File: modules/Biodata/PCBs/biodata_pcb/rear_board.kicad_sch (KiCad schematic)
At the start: 7 parts, among them U1 NE555P

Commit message: Working on biodata layout and PCB
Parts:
- added A1: Arduino_Nano_v3.x, Module:Arduino_Nano, symbol MCU_Module:Arduino_Nano_v3.x
- added C4: 100nF, symbol Device:C
- added C5: 10uF, Capacitor_THT:CP_Radial_D4.0mm_P1.50mm, symbol Device:C_Polarized_US
- added J10: Eurorack_2x8_Power, Connector_IDC:IDC-Header_2x08_P2.54mm_Vertical, symbol FreeModular:Eurorack_2x8_Power
- added Q1, Q2: 2N3904, Package_TO_SOT_THT:TO-92L_Inline_Wide, symbol Device:Q_NPN_EBC
- added R4, R5, R6, R7: 100kΩ, Resistor_THT:R_Axial_DIN0207_L6.3mm_D2.5mm_P10.16mm_Horizontal, symbol Device:R
- added R8, R9: 1kΩ, Resistor_THT:R_Axial_DIN0207_L6.3mm_D2.5mm_P10.16mm_Horizontal, symbol Device:R
- added U2: MCP4922, Package_DIP:DIP-14_W7.62mm, symbol Analog_DAC:MCP4922
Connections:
- net +5V: now also A1.27 (+5V), C4.2, C5.1, J10.11 (+5v), J10.12 (+5v), U2.1 (Vdd), U2.11 (VrefB), U2.13 (VrefA), U2.9 (~{SHDN})
- net GND: now also A1.29 (GND), A1.4 (GND), C4.1, C5.2, J10.3 (GND), J10.4 (GND), J10.5 (GND), J10.6 (GND), J10.7 (GND), J10.8 (GND), Q1.1 (E), Q2.1 (E), R5.1, R7.1, U2.12 (Vss), U2.8 (~{LDAC})
- net pulse_out: now also A1.5 (D2)
- net probe_pos: now reaches R2.1
- net probe_neg: now reaches R3.1
- new net: Q1.2 (B), R4.2, R5.2
- new net: J10.1 (-12v), J10.2 (-12v)
- new net: J10.10 (+12v), J10.9 (+12v)
- new net: R9.1, U2.10 (VB)
- new net: R8.1, U2.14 (VA)
- new net: Q2.2 (B), R6.2, R7.2
- new net DAC_CS: A1.13 (D10), U2.3 (~{CS})
- new net SPI_SCK: A1.16 (D13), U2.4 (SCK)
- new net SPI_SDI: A1.14 (D11), U2.5 (SDI)
- new net cv_out_a: R8.2
- new net cv_out_b: R9.2
- new net density: A1.22 (A3)
- new net gate_in_a: R4.1
- new net gate_in_a_buffered: A1.6 (D3), Q1.3 (C)
- new net gate_in_b: R6.1
- new net gate_in_b_buffered: A1.7 (D4), Q2.3 (C)
- new net gate_out_a: A1.8 (D5)
- new net gate_out_b: A1.9 (D6)
- new net sensitivity: A1.21 (A2)
- new net slew_a: A1.23 (A4)
- new net slew_b: A1.24 (A5)
- new net spread_a: A1.25 (A6)
- new net spread_b: A1.26 (A7)
- no-connect marks 0 -> 15
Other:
- note added: "with internal pullup to 5v"
- moved on the sheet: C1, C2, C3, R1, R2, R3, U1

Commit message: v0.1 biodata pcb
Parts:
- removed C1: 10nF, symbol Device:C
- removed C2: 1nF, symbol Device:C
- removed C3: 100nF, symbol Device:C
- removed R1: 1kΩ, symbol Device:R
- removed R2, R3: 1MΩ, symbol Device:R
- removed U1: NE555P, Package_DIP:DIP-8_W7.62mm, symbol Timer:NE555P
- added C10, C11, C8, C9: 100pF, Capacitor_THT:C_Disc_D4.7mm_W2.5mm_P5.00mm, symbol Device:C_Small
- added C14, C5, C6, C7: 100nF, Capacitor_THT:C_Disc_D4.7mm_W2.5mm_P5.00mm, symbol Device:C
- added Q3, Q4: 2N3904, Package_TO_SOT_THT:TO-92L_Inline_Wide, symbol Device:Q_NPN_EBC
- added R18, R19, R20, R21, R30, R32: 1kΩ, Resistor_THT:R_Axial_DIN0207_L6.3mm_D2.5mm_P10.16mm_Horizontal, symbol Device:R
- added R22, R23, R24, R25, R26, R27, R28, R29, R31: 10kΩ, Resistor_THT:R_Axial_DIN0207_L6.3mm_D2.5mm_P10.16mm_Horizontal, symbol Device:R
- added U5: MCP4922, Package_DIP:DIP-14_W7.62mm, symbol Analog_DAC:MCP4922
- added U6: TL074, Package_DIP:DIP-14_W7.62mm, symbol Amplifier_Operational:TL074
- C4: footprint (none) -> Capacitor_THT:C_Disc_D4.7mm_W2.5mm_P5.00mm
- R8, R9: value 1kΩ -> 100kΩ
- renumbered C5 to C13, J10 to J13
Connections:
- net +5V: now also C5.2, C6.2, R30.2, U5.1 (Vdd), U5.11 (VrefB), U5.13 (VrefA), U5.9 (~{SHDN})
- net GND: now also R9.1, C14.2, C5.1, C6.1, C7.1, Q3.1 (E), Q4.1 (E), R22.1, R24.1, R26.1, R28.1, U5.12 (Vss), U5.8 (~{LDAC})
- net SPI_SCK: now also U5.4 (SCK)
- net SPI_SDI: now also U5.5 (SDI)
- net cv_out_a: now also R19.2, R25.2; no longer R8.2
- net cv_out_b: now also R20.2, R27.2; no longer R9.2
- net density: now also A1.20 (A1); no longer A1.22 (A3)
- net gate_out_a: now also A1.9 (D6); no longer A1.8 (D5)
- net gate_out_b: now also A1.10 (D7); no longer A1.9 (D6)
- net pulse_out: now also R32.2; no longer A1.5 (D2)
- net sensitivity: now also A1.19 (A0); no longer A1.21 (A2)
- net slew_a: now also A1.22 (A3); no longer A1.23 (A4)
- net spread_a: now also A1.21 (A2); no longer A1.25 (A6)
- net spread_b: now also A1.23 (A4); no longer A1.26 (A7)
- net gate_out_c: now reaches A1.11 (D8)
- net DAC_CS_1: now reaches A1.12 (D9)
- net DAC_CS_1: now also U2.3 (~{CS})
- net -12V: now reaches J13.1 (-12v), J13.2 (-12v)
- net -12V: now also C14.1, U6.4 (V+)
- net +12V: now reaches J13.10 (+12v), J13.9 (+12v)
- net +12V: now also C7.2, U6.11 (V-)
- net prescale_cv: now reaches U2.10 (VB)
- net prescale_cv: now also U6.3 (+); no longer R9.1
- net gate_in_c: now reaches R8.1
- net gate_in_c: no longer U2.14 (VA)
- net DAC_CS renamed DAC_CS_2
- net DAC_CS_2: now also U5.3 (~{CS}); no longer U2.3 (~{CS})
- new net: Q3.2 (B), R8.2, R9.2
- new net: C8.1, R22.2, R23.1, U6.2 (-)
- new net: C10.1, R26.2, R27.1, U6.9 (-)
- new net: Q4.2 (B), R31.1
- new net: C8.2, R18.1, U6.1
- new net: C9.1, R24.2, R25.1, U6.6 (-)
- new net: C9.2, R19.1, U6.7
- new net: C10.2, R20.1, U6.8
- new net: C11.1, R28.2, R29.1, U6.13 (-)
- new net: C11.2, R21.1, U6.14
- new net Isolated Section/pulse_out: R31.2
- new net cv_out: R18.2, R23.2
- new net cv_out_c: R21.2, R29.2
- new net gate_in_c_buffered: A1.8 (D5), Q3.3 (C)
- new net prescale_cv_a: U2.14 (VA), U6.5 (+)
- new net prescale_cv_b: U5.10 (VB), U6.10 (+)
- new net prescale_cv_c: U5.14 (VA), U6.12 (+)
- new net pulse_signal: A1.5 (D2), Q4.3 (C), R30.1, R32.1
- new net slew_c: A1.26 (A7)
- new net spread_c: A1.25 (A6)
- no-connect marks 15 -> 8
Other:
- added sheet Isolated Section (isolated_section.kicad_sch)
- company: (none) -> Free Modular
- title: (none) -> Biodata
- moved on the sheet: C13, C4, J13, U2

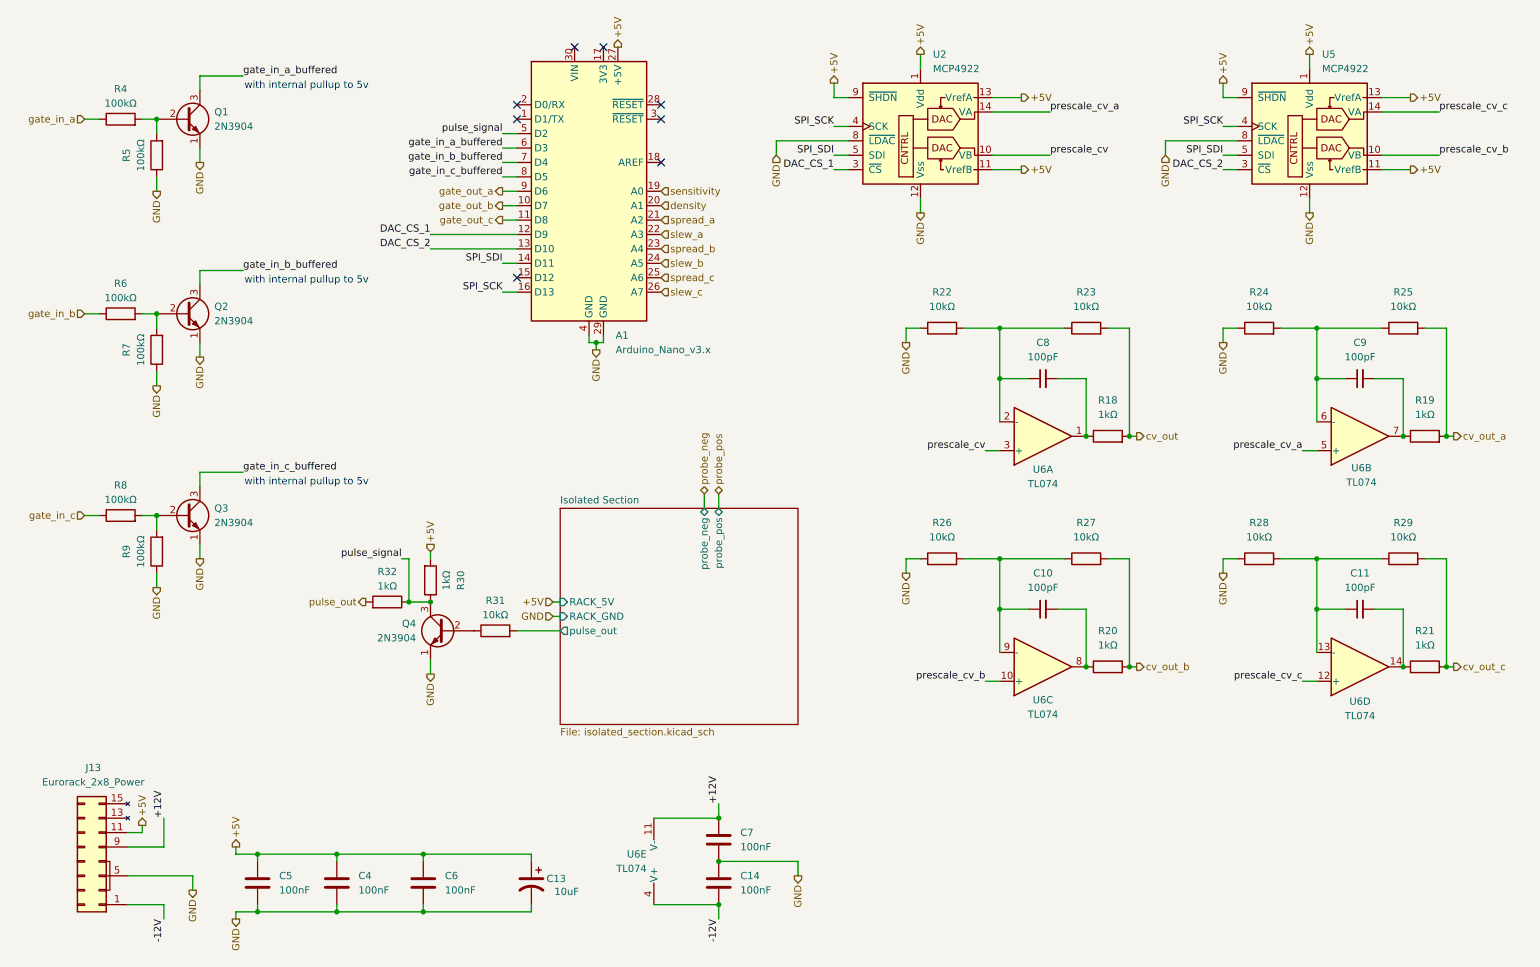
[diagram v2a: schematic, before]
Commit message: Switch biodata to monophonic
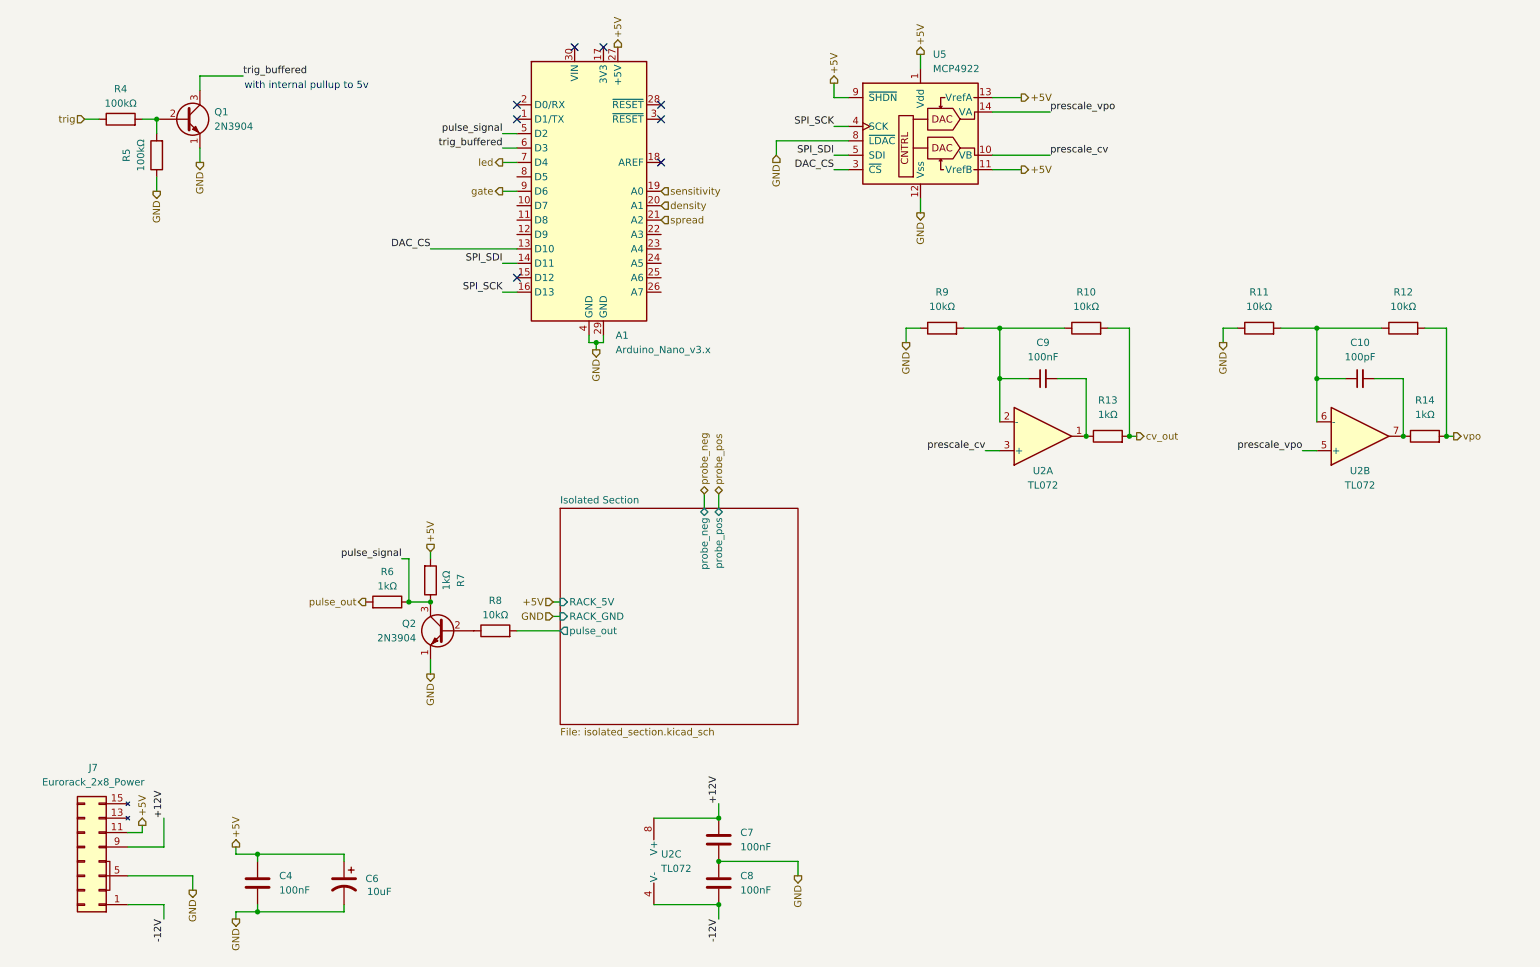
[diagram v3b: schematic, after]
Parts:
- removed C10, C11: 100pF, Capacitor_THT:C_Disc_D4.7mm_W2.5mm_P5.00mm, symbol Device:C_Small
- removed C4, C6: 100nF, Capacitor_THT:C_Disc_D4.7mm_W2.5mm_P5.00mm, symbol Device:C
- removed Q2, Q3: 2N3904, Package_TO_SOT_THT:TO-92L_Inline_Wide, symbol Device:Q_NPN_EBC
- removed R20, R21: 1kΩ, Resistor_THT:R_Axial_DIN0207_L6.3mm_D2.5mm_P10.16mm_Horizontal, symbol Device:R
- removed R26, R27, R28, R29: 10kΩ, Resistor_THT:R_Axial_DIN0207_L6.3mm_D2.5mm_P10.16mm_Horizontal, symbol Device:R
- removed R6, R7, R8, R9: 100kΩ, Resistor_THT:R_Axial_DIN0207_L6.3mm_D2.5mm_P10.16mm_Horizontal, symbol Device:R
- removed U5: MCP4922, Package_DIP:DIP-14_W7.62mm, symbol Analog_DAC:MCP4922
- removed U6: TL074, Package_DIP:DIP-14_W7.62mm, symbol Amplifier_Operational:TL074
- added U2: TL072, Package_DIP:DIP-8_W7.62mm, symbol Amplifier_Operational:TL072
- C9: renamed from C8; value 100pF -> 100nF
- renumbered C9 to C10, C5 to C4, C13 to C6, C14 to C8, J13 to J7, Q4 to Q2, R23 to R10, R24 to R11, R25 to R12, R18 to R13, R19 to R14, R32 to R6, R30 to R7, R31 to R8, R22 to R9, U2 to U5
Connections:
- net +12V: now also U2.8 (V+)
- net -12V: now also U2.4 (V-)
- net prescale_cv: now also U2.3 (+)
- net at C9.1, R10.1, R9.2: now also U2.2 (-)
- net at C9.2, R13.1: now also U2.1
- net at C10.1, R11.2, R12.1: now also U2.6 (-)
- net at C10.2, R14.1: now also U2.7
- net DAC_CS_1: no longer names the net of A1.12 (D9)
- net DAC_CS_1: no longer U5.3 (~{CS})
- net DAC_CS_2 renamed DAC_CS
- net DAC_CS: now also U5.3 (~{CS})
- net cv_out_a renamed vpo
- net gate_in_a renamed trig
- net gate_in_a_buffered renamed trig_buffered
- net gate_in_b_buffered renamed led
- net gate_in_c_buffered: no longer names the net of A1.8 (D5)
- net gate_out_a renamed gate
- net gate_out_b: no longer names the net of A1.10 (D7)
- net gate_out_c: no longer names the net of A1.11 (D8)
- net prescale_cv_a renamed prescale_vpo
- net prescale_vpo: now also U2.5 (+)
- net slew_a: no longer names the net of A1.22 (A3)
- net slew_b: no longer names the net of A1.24 (A5)
- net slew_c: no longer names the net of A1.26 (A7)
- net spread_a renamed spread
- net spread_b: no longer names the net of A1.23 (A4)
- net spread_c: no longer names the net of A1.25 (A6)
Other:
- moved on the sheet: C6

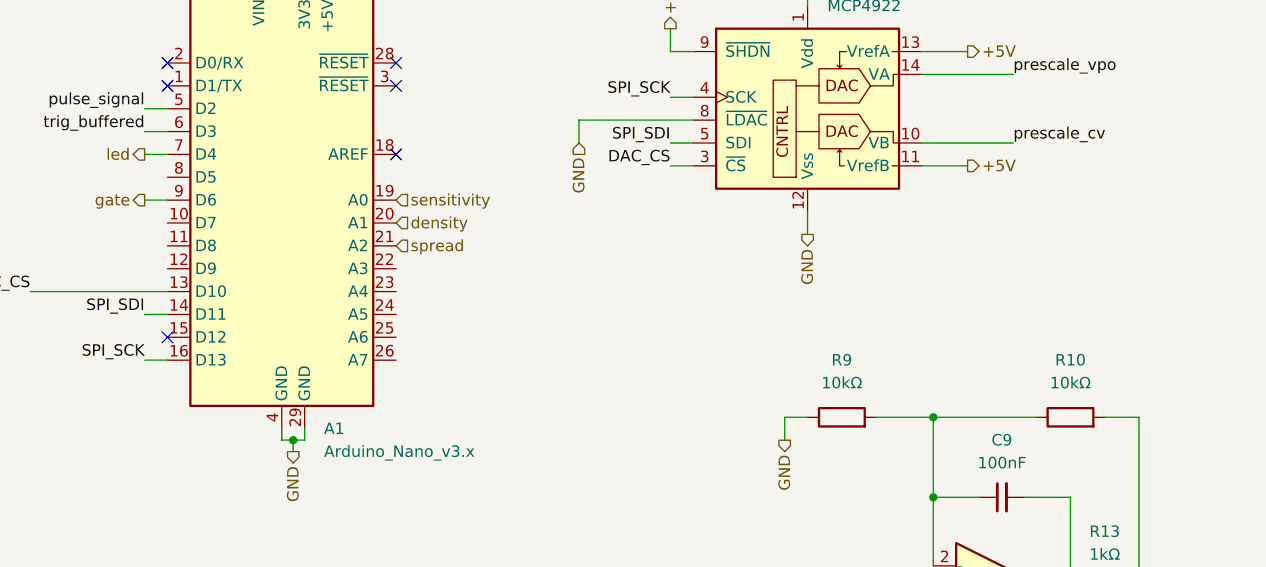
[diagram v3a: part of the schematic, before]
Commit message: Rearrange biodata PCB to allow mounting bolt; update CV algorithm
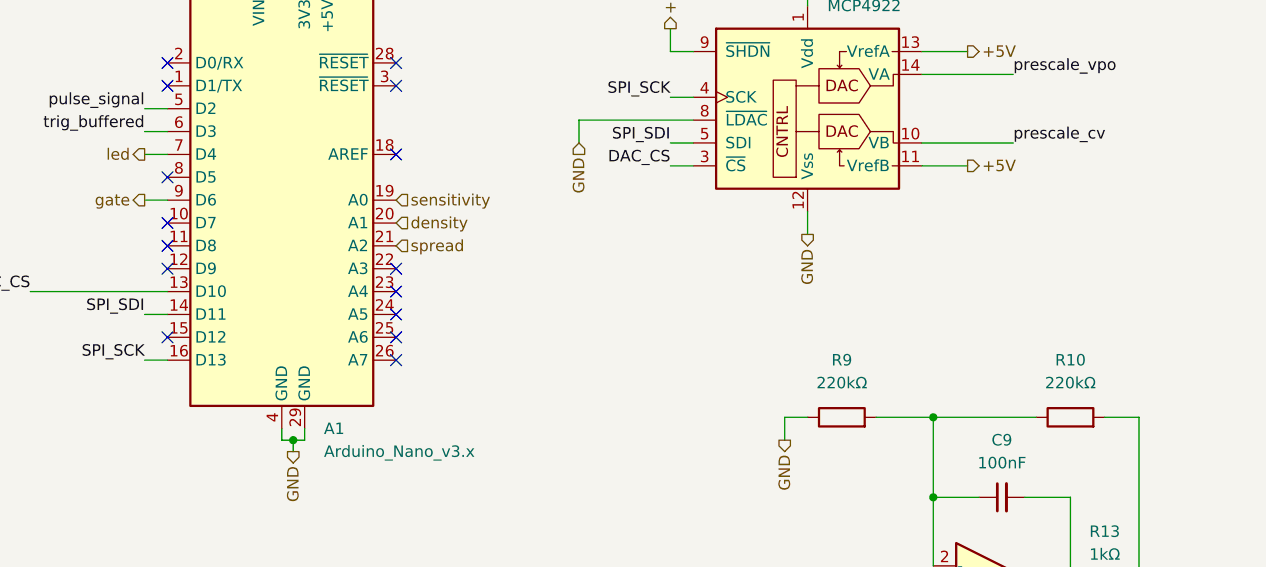
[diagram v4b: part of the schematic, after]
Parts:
- R10, R9: value 10kΩ -> 220kΩ
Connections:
- no-connect marks 8 -> 17
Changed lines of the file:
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@@
+	)
+	(no_connect
+		(at 129.54 74.93)
+	)
+	(no_connect
+		(at 129.54 67.31)
+	)
+	(no_connect
+		(at 104.14 54.61)
 	)
 	(no_connect
@@
 	)
 	(no_connect
+		(at 104.14 59.69)
+	)
+	(no_connect
 		(at 129.54 44.45)
+	)
+	(no_connect
+		(at 129.54 69.85)
+	)
+	(no_connect
+		(at 104.14 62.23)
 	)
 	(no_connect
@@
 	)
 	(no_connect
+		(at 129.54 72.39)
+	)
+	(no_connect
+		(at 129.54 64.77)
+	)
+	(no_connect
 		(at 119.38 31.75)
+	)
+	(no_connect
+		(at 104.14 64.77)
 	)
 	(wire
@@
 			)
 		)
-		(property "Value" "10kΩ"
+		(property "Value" "220kΩ"
 			(at 204.47 77.47 90)
 			(effects
@@
 			)
 		)
-		(property "Value" "10kΩ"
+		(property "Value" "220kΩ"
 			(at 179.07 77.47 90)
 			(effects
